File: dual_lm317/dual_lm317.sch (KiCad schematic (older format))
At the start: 18 parts, among them J1 Conn_01x02_Male, J2 Conn_01x02_Male, U1 LM317_TO-220, U2 LT3080xST, U3 LT3080xST

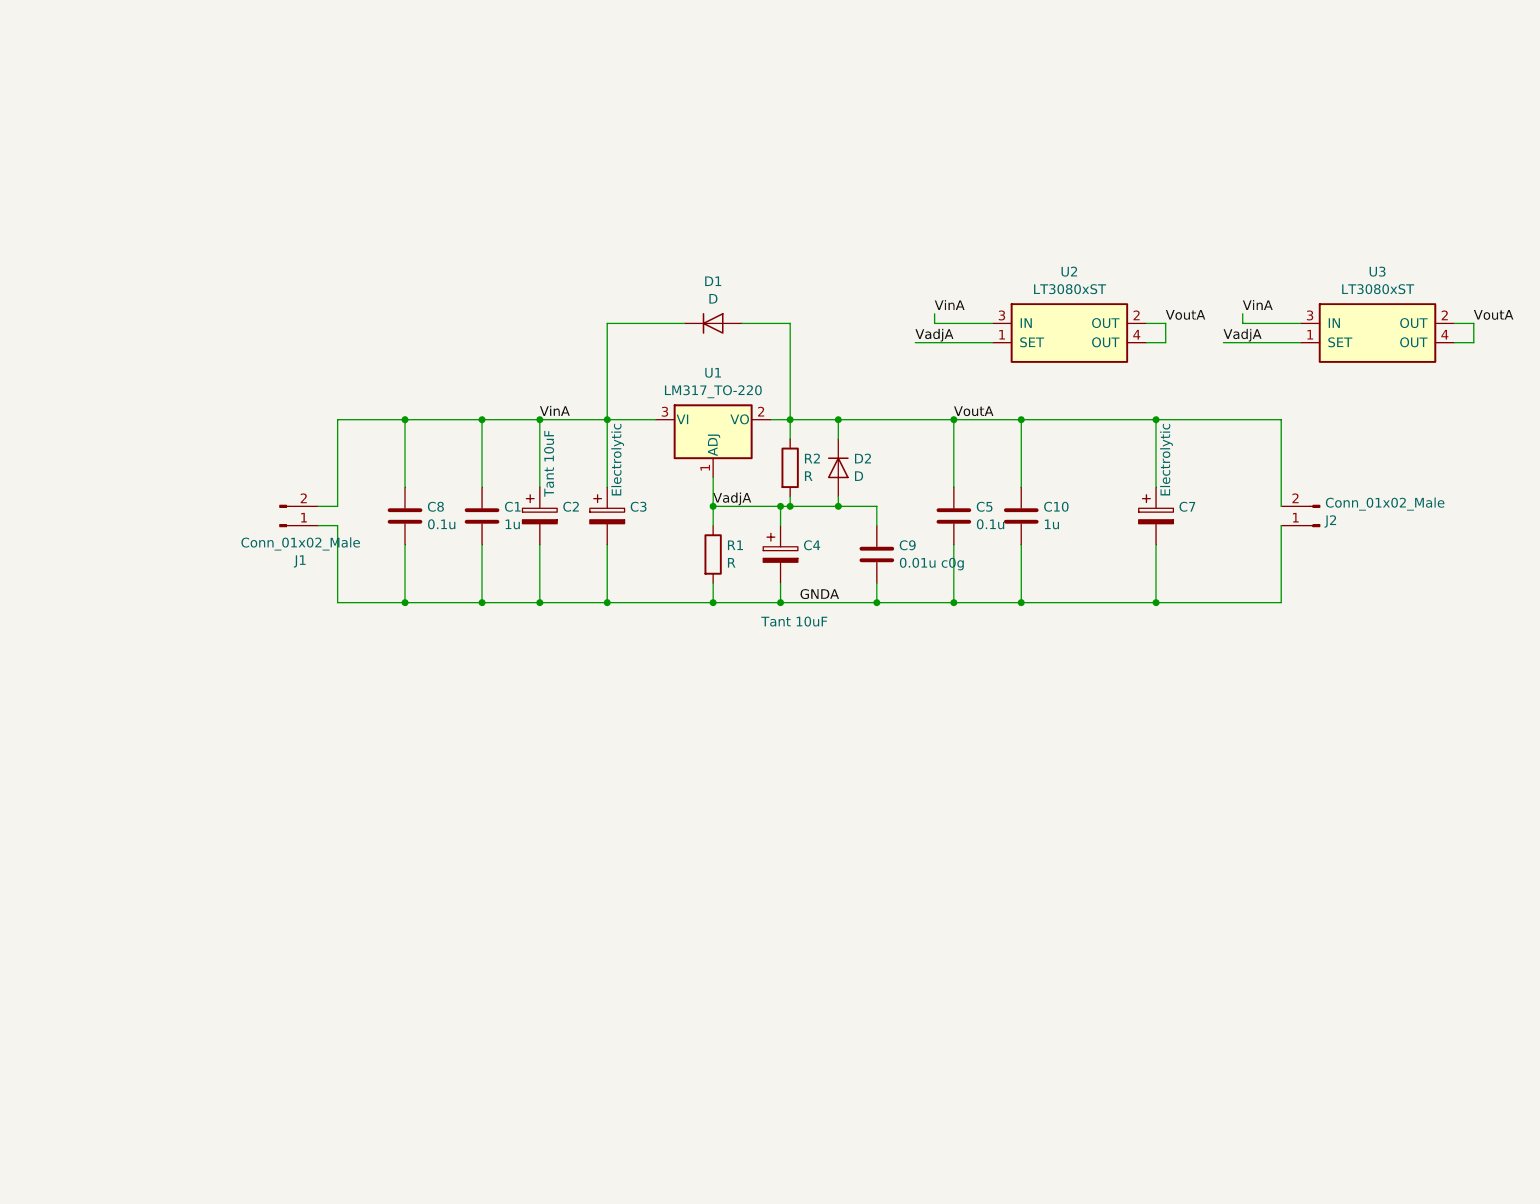
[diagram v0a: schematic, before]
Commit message: migrate heirachycal sheets
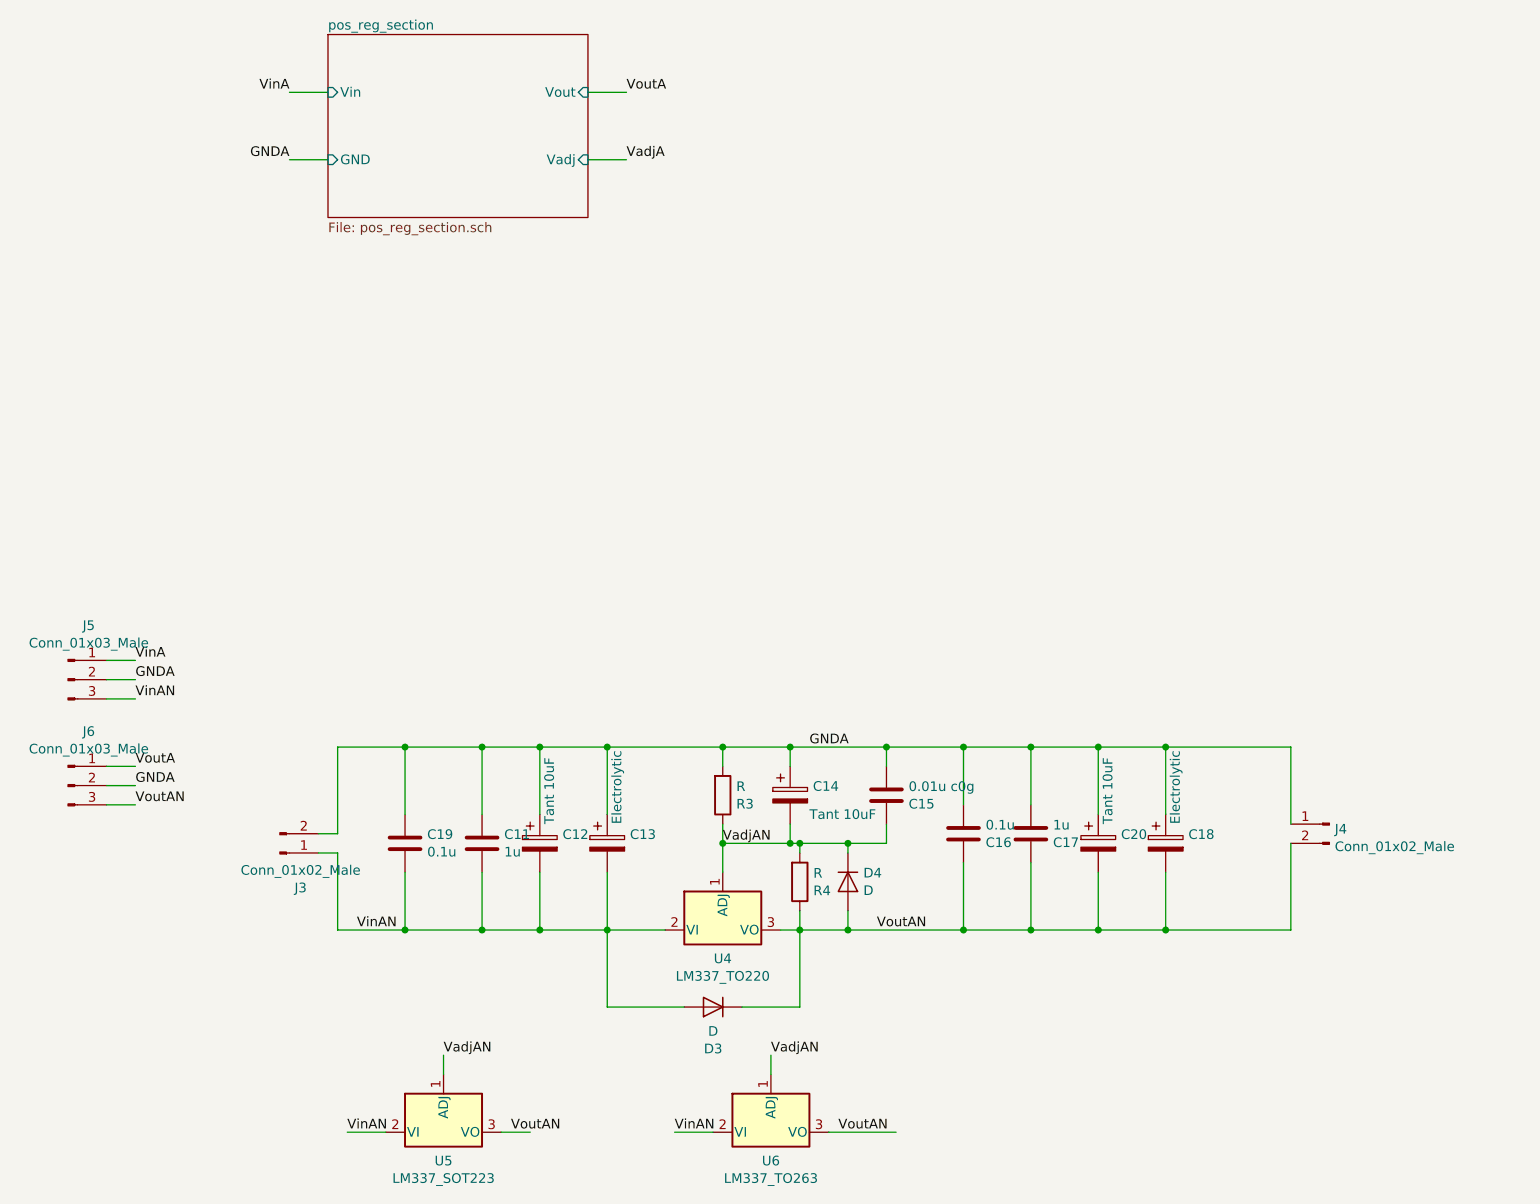
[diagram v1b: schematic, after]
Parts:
- removed C1, C10: 1u, Capacitor_SMD:C_1206_3216Metric_Pad1.33x1.80mm_HandSolder, symbol Device:C
- removed C2, C4: Tant 10uF, Capacitor_Tantalum_SMD:CP_EIA-6032-15_Kemet-U_Pad2.25x2.35mm_HandSolder, symbol Device:CP
- removed C3, C7: Electrolytic, Capacitor_SMD:CP_Elec_8x10.5, symbol Device:CP
- removed C5, C8: 0.1u, Capacitor_SMD:C_0805_2012Metric_Pad1.18x1.45mm_HandSolder, symbol Device:C
- removed C9: 0.01u c0g, Capacitor_SMD:C_1206_3216Metric_Pad1.33x1.80mm_HandSolder, symbol Device:C
- removed D1, D2: D, Diode_SMD:D_SOD-323, symbol Device:D
- removed J1, J2: Conn_01x02_Male, Connector_PinHeader_2.54mm:PinHeader_1x02_P2.54mm_Vertical, symbol Connector:Conn_01x02_Male
- removed R1, R2: R, Resistor_SMD:R_1206_3216Metric_Pad1.30x1.75mm_HandSolder, symbol Device:R
- removed U1: LM317_TO-220, Package_TO_SOT_THT:TO-220-3_Horizontal_TabDown, symbol Regulator_Linear:LM317_TO-220
- removed U2: LT3080xST, Package_TO_SOT_SMD:SOT-223, symbol Regulator_Linear:LT3080xST
- removed U3: LT3080xST, Package_TO_SOT_SMD:TO-263-3_TabPin4, symbol Regulator_Linear:LT3080xST
- added C11, C17: 1u, Capacitor_SMD:C_1206_3216Metric_Pad1.42x1.75mm_HandSolder, symbol Device:C
- added C12, C14, C20: Tant 10uF, Capacitor_Tantalum_SMD:CP_EIA-6032-15_Kemet-U_Pad2.25x2.35mm_HandSolder, symbol Device:CP
- added C13, C18: Electrolytic, Capacitor_SMD:CP_Elec_8x10.5, symbol Device:CP
- added C15: 0.01u c0g, Capacitor_SMD:C_1206_3216Metric_Pad1.42x1.75mm_HandSolder, symbol Device:C
- added C16, C19: 0.1u, Capacitor_SMD:C_0805_2012Metric_Pad1.15x1.40mm_HandSolder, symbol Device:C
- added D3, D4: D, Diode_SMD:D_SOD-323, symbol Device:D
- added J3, J4: Conn_01x02_Male, Connector_PinHeader_2.54mm:PinHeader_1x02_P2.54mm_Vertical, symbol Connector:Conn_01x02_Male
- added J5, J6: Conn_01x03_Male, Connector_PinHeader_2.54mm:PinHeader_1x03_P2.54mm_Vertical, symbol Connector:Conn_01x03_Male
- added R3, R4: R, Resistor_SMD:R_1206_3216Metric_Pad1.42x1.75mm_HandSolder, symbol Device:R
- added U4: LM337_TO220, Package_TO_SOT_THT:TO-220-3_Horizontal_TabDown, symbol Regulator_Linear:LM337_TO220
- added U5: LM337_SOT223, Package_TO_SOT_SMD:SOT-223-3_TabPin2, symbol Regulator_Linear:LM337_SOT223
- added U6: LM337_TO263, Package_TO_SOT_SMD:TO-263-2, symbol Regulator_Linear:LM337_TO263
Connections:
- net GNDA: now also C11.1, C12.1, C13.1, C14.1, C15.2, C16.2, C17.2, C18.1, C19.1, C20.1, J3.2 (Pin_2), J4.1 (Pin_1), J5.2 (Pin_2), J6.2 (Pin_2), R3.2
- net VinA: now also J5.1 (Pin_1)
- net VoutA: now also J6.1 (Pin_1)
- new net VadjAN: C14.2, C15.1, D4.1 (K), R3.1, R4.2, U4.1 (ADJ), U5.1 (ADJ), U6.1 (ADJ)
- new net VinAN: C11.2, C12.2, C13.2, C19.2, D3.2 (A), J3.1 (Pin_1), J5.3 (Pin_3), U4.2 (VI), U5.2 (VI), U6.2 (VI)
- new net VoutAN: C16.1, C17.1, C18.2, C20.2, D3.1 (K), D4.2 (A), J4.2 (Pin_2), J6.3 (Pin_3), R4.1, U4.3 (VO), U5.3 (VO), U6.3 (VO)

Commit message: Relay array board; Last checkup; Gerberfile updates
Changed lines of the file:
@@
 $Descr A4 11693 8268
 encoding utf-8
-Sheet 1 2
+Sheet 1 3
 Title ""
 Date ""
@@
 Wire Wire Line
 	2450 2050 2650 2050
+$Sheet
+S 6100 1950 1350 950
+U 613B0780
+F0 "pos_reg_B" 50
+F1 "pos_reg_section.sch" 50
+F2 "Vin" I L 6100 2250 50
+F3 "Vout" I R 7450 2250 50
+F4 "GND" I L 6100 2600 50
+F5 "Vadj" I R 7450 2600 50
+$EndSheet
+Text Label 5900 2250 2    50   ~ 0
+VinB
+Text Label 5900 2600 2    50   ~ 0
+GNDB
+Text Label 7650 2250 0    50   ~ 0
+VoutB
+Text Label 7650 2600 0    50   ~ 0
+VadjB
+Wire Wire Line
+	7650 2600 7450 2600
+Wire Wire Line
+	7450 2250 7650 2250
+Wire Wire Line
+	6100 2250 5900 2250
+Wire Wire Line
+	5900 2600 6100 2600
 $EndSCHEMATC
